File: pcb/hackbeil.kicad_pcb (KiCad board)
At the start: 2 copper layers, 138.5 x 116.3 mm, 71 parts

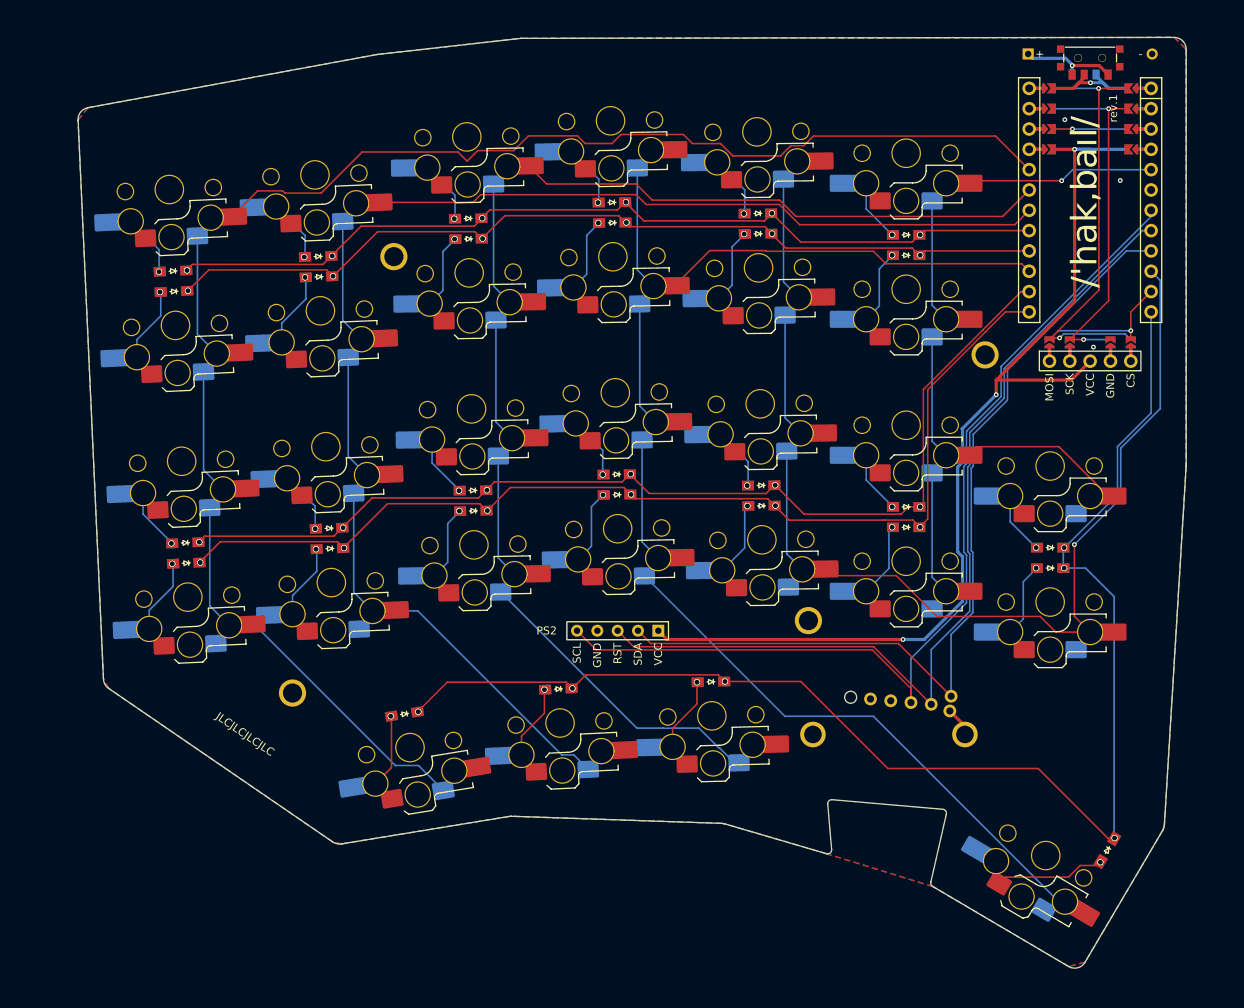
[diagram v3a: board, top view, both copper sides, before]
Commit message: Add teardrops
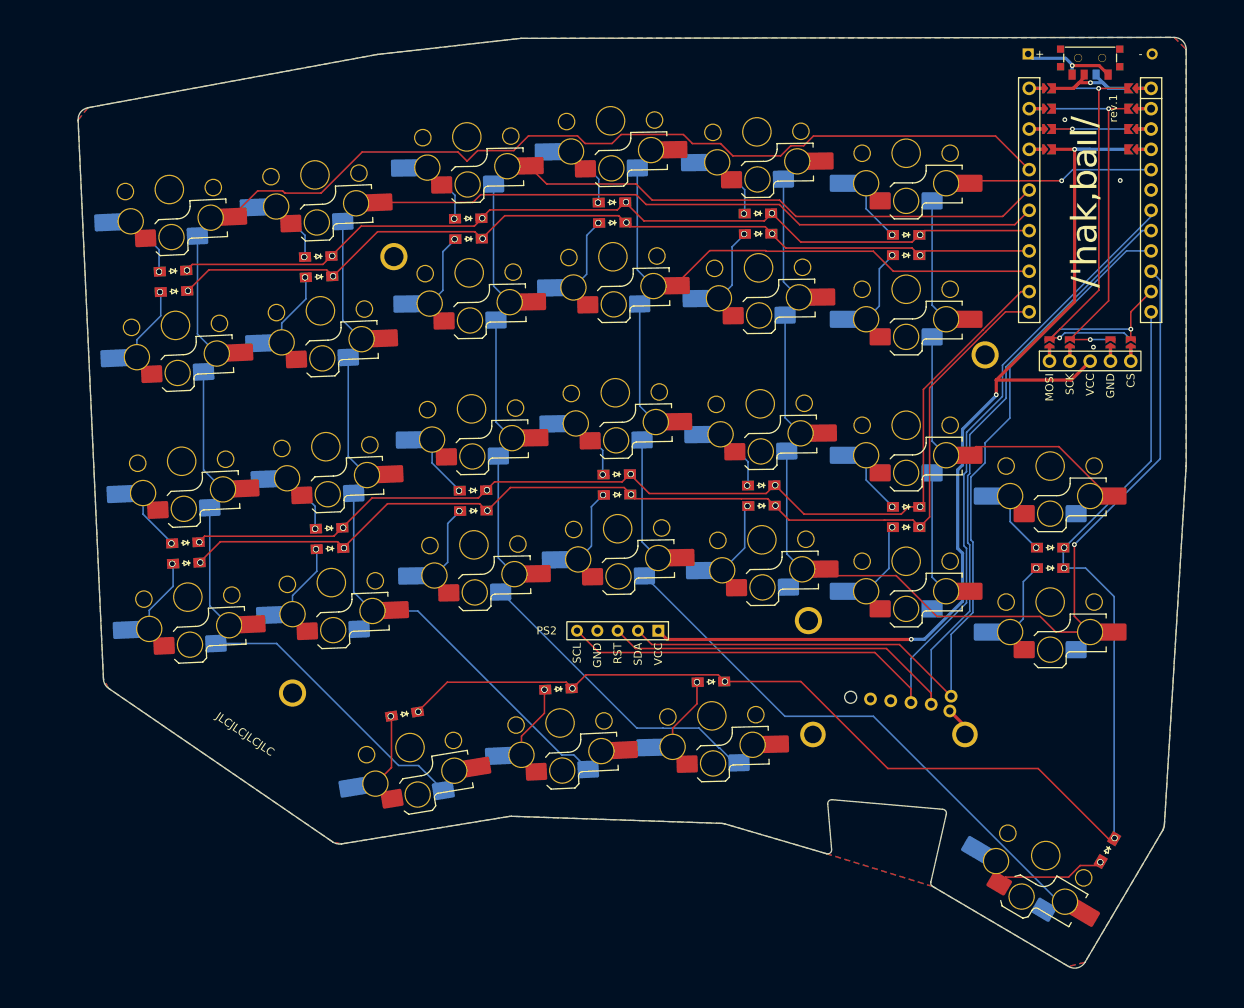
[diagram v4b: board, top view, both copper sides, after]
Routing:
- net TP_RST: track 114.5 -> 115.3 mm
- net COL0: track 192.2 -> 192.9 mm

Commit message: Fancy rounded tracks (thanks, Mitxela!)
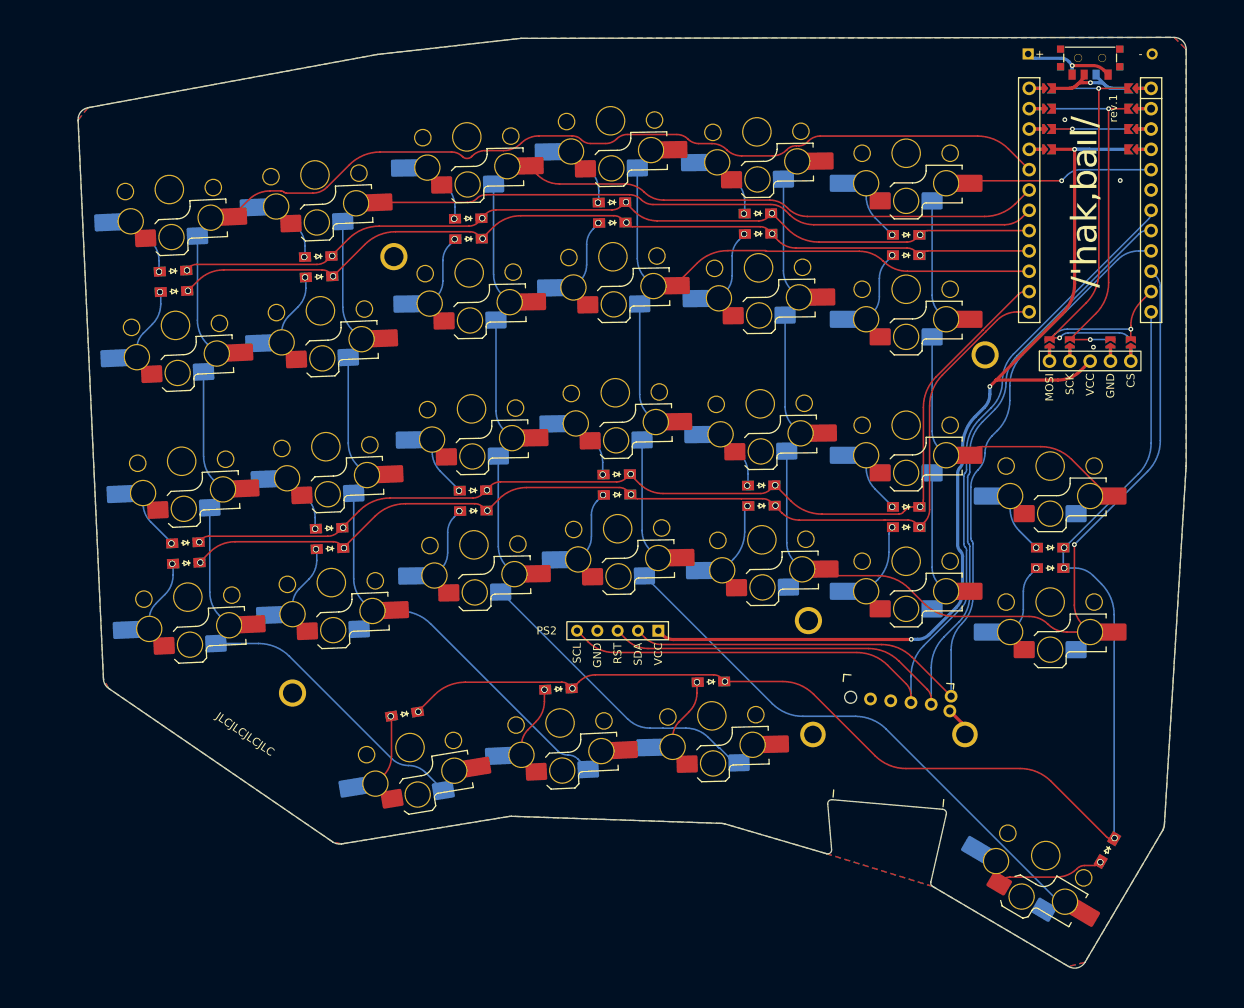
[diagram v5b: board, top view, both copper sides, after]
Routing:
- net COL0: track 192.9 -> 188.9 mm
- net ROW4: track 172.9 -> 170.8 mm
- net COL1: track 166.4 -> 164.4 mm
- net COL2: track 152.1 -> 150.0 mm
- net TP_SDA: track 110.6 -> 108.5 mm
- net COL4: track 134.2 -> 132.3 mm
- net TP_RST: track 115.3 -> 113.4 mm
- net TP_SCL: track 120.7 -> 118.9 mm
- net ROW3: track 131.9 -> 130.1 mm
- net COL3: track 163.4 -> 161.7 mm
- net ROW2: track 130.0 -> 128.3 mm
- net ROW0: track 112.4 -> 110.7 mm
- net ROW1: track 112.7 -> 111.1 mm
- net VCC: track 127.5 -> 126.1 mm
- net COL5: track 91.6 -> 90.7 mm
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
